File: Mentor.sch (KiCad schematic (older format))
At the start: 35 parts

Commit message: Mentor Schematic, V1.0
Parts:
- removed J?: CONN_01X04, symbol CONN_01X04
- added J2: CONN_01X05, symbol CONN_01X05
- added J7: CONN_01X18, symbol CONN_01X18
- added R9: 100R, symbol R
- added RV1: 10k, symbol POT
- gave numbers to parts that had none: 34
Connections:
- wire segments 114 -> 129
- no-connect marks 1 -> 6
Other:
- note added: "4x40 Display"
- note added: "DB0"
- note added: "DB1"
- note added: "DB2"
- note added: "DB3"
- note added: "DB4"
- note added: "DB5"
- note added: "DB6"
- note added: "DB7\n"
- note added: "E1"
- note added: "E2"
- note added: "From Alexandrie\nControl board"
- note added: "LedA"
- note added: "LedK"
- note added: "Mentor"
- note added: "Mentor\nA power/U/I/VSWR/Temp. indicator\nfor the Hermes SDR familly"
- note added: "PTT\ndisable"
- note added: "RS\n"
- note added: "RW\n"
- note added: "VO"
- note added: "VSS"
- note added: "Vdd"
- note added: "Vee"
- note removed: "Alexandrite"
- note removed: "Alexandrite, the ever changing color gem \nA power/U/I/VSWR/Temp. indicator\nfor the Hermes SDR familly"
- note removed: "From TX/RX_Relay\nControl board"
- note removed: "reporter\n le pinout \nsur ctrl board \nAlexandrie\n"

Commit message: final schematic drawing
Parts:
- removed J2: CONN_01X05, symbol CONN_01X05
- removed J3: CONN_01X03, symbol CONN_01X03
- added J2: CONN_01X06, symbol CONN_01X06
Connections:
- wire segments 129 -> 134
- no-connect marks 6 -> 17
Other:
- note added: "<--C°"
- note added: "<--I"
- note added: "<--U"
- note added: "From Amp"
- note added: "Mentor\nA power/U/I/VSWR/Temp. indicator\nand security system\nfor the Hermes SDR familly"
- note added: "ptt disable/\n <-- Active Bias\n"
- note removed: "Mentor\nA power/U/I/VSWR/Temp. indicator\nfor the Hermes SDR familly"
- note removed: "ptt disable\n"
- moved on the sheet: L1, R1

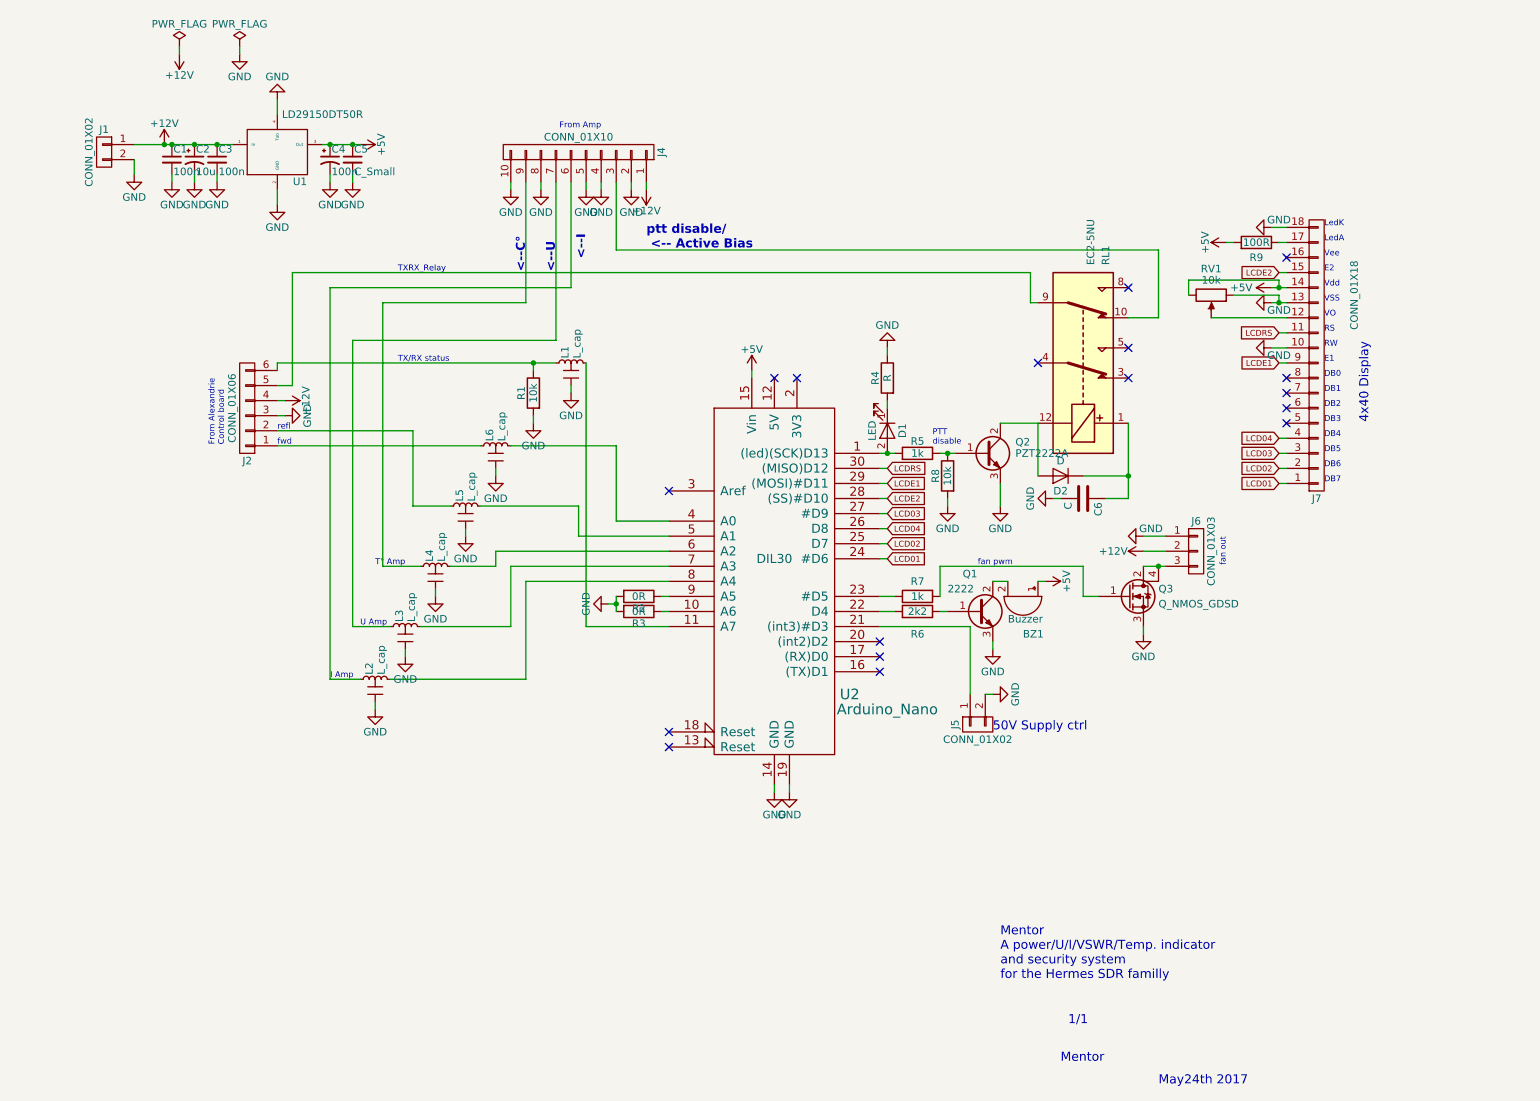
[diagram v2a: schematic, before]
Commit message: Mentor pcb routed, minor errors fixed
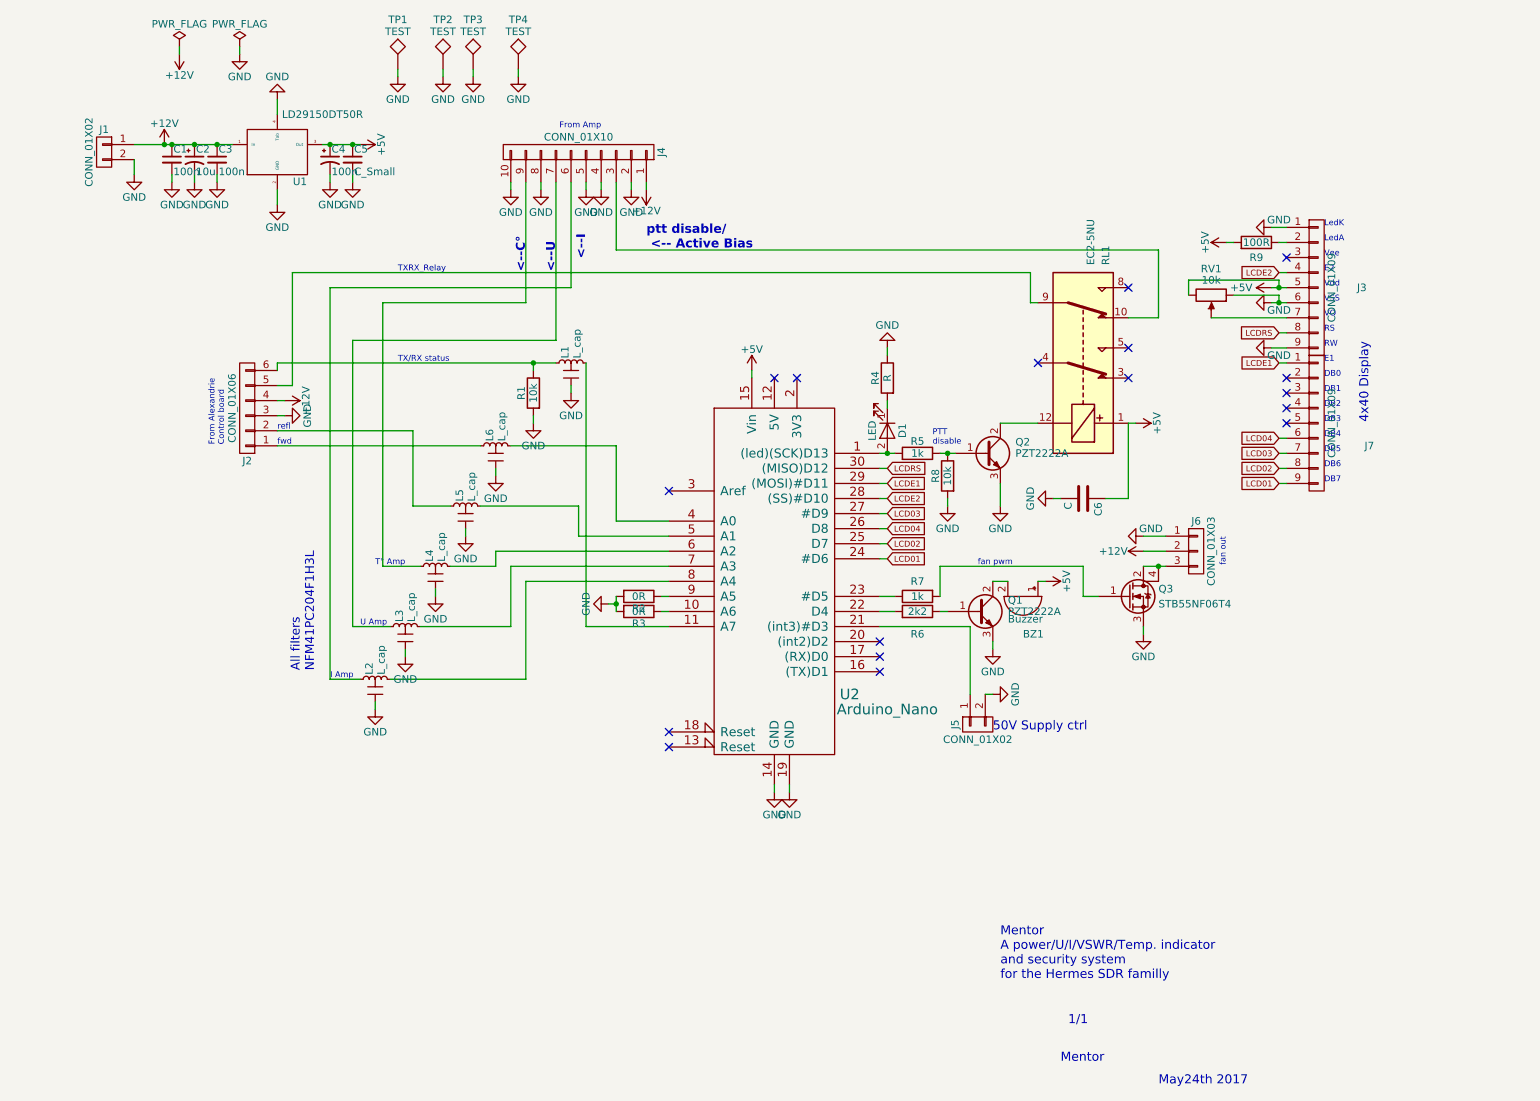
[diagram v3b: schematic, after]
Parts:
- removed D2: D, symbol D
- removed J7: CONN_01X18, symbol CONN_01X18
- added J3, J7: CONN_01X09, conn_kk100:kk100_22-23-2091, symbol CONN_01X09
- added TP1, TP2, TP3, TP4: TEST, Mounting_Holes:MountingHole_3.5mm_Pad, symbol TEST
- BZ1: footprint (none) -> Buzzers_Beepers:MagneticBuzzer_Kingstate_KCG0601
- C1, C3, C4, C5, C6: footprint (none) -> Capacitors_SMD:C_0805_HandSoldering
- C2: footprint (none) -> Capacitors_Tantalum_SMD:CP_Tantalum_Case-C_EIA-6032-28_Hand
- D1: footprint (none) -> Diodes_SMD:D_0805
- J1, J5: footprint (none) -> conn_kk100:kk100_22-23-2021
- J2: footprint (none) -> conn_kk100:kk100_22-23-2061
- J4: footprint (none) -> conn_kk100:kk100_22-23-2101
- J6: footprint (none) -> conn_kk100:kk100_22-23-2031
- L1, L2, L3, L4, L5, L6: footprint (none) -> Ferrite_LC_NFM41P:Ferrite_LC_NFM41P
- Q1: value 2222 -> PZT2222A
- Q3: value Q_NMOS_GDSD -> STB55NF06T4; footprint (none) -> TO_SOT_Packages_SMD:TO-263-3_TabPin4
- R1, R2, R3, R4, R5, R6, R7, R8, R9: footprint (none) -> Resistors_SMD:R_0805_HandSoldering
- RL1: footprint (none) -> 2_Form_C_Relay:smd_2_formC
- RV1: footprint (none) -> Trimmer_3314G1_Handsoldering:Trimmer_3314G1_Handsoldering
- U1: footprint (none) -> TO_SOT_Packages_SMD:SOT-223
- U2: footprint DIL30 -> arduino_nano:arduino_nano
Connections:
- net +5V: now also C6.1, RL1.1, J3.5 (P5)
- net GND: now also J3.1 (P1), J3.6 (P6), J3.9 (P9), TP1.1, TP2.1, TP3.1, TP4.1
- net LCD01: now also J7.9 (P9)
- net LCD02: now also J7.8 (P8)
- net LCD03: now also J7.7 (P7)
- net LCD04: now also J7.6 (P6)
- net LCDE1: now also J7.1 (P1)
- net LCDE2: now also J3.4 (P4)
- net LCDRS: now also J3.8 (P8)
- net at RV1.2: now also J3.7 (P7)
- net at R9.1: now also J3.2 (P2)
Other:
- note added: "All filters \nNFM41PC204F1H3L\n"

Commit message: RTM, silmask to do
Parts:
- C5: value C_Small -> 100n
- U1: footprint TO_SOT_Packages_SMD:SOT-223 -> TO_SOT_Packages_SMD:TO-263-3_TabPin4
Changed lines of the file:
@@
 F 0 "U1" H 2400 1254 50  0000 C CNN
 F 1 "LD29150DT50R" H 2550 1700 50  0000 C CNN
-F 2 "TO_SOT_Packages_SMD:SOT-223" H 2250 1450 50  0001 C CNN
+F 2 "TO_SOT_Packages_SMD:TO-263-3_TabPin4" H 2250 1450 50  0001 C CNN
 F 3 "" H 2250 1450 50  0001 C CNN
 	1    2250 1450
@@
 P 2750 1500
 F 0 "C5" H 2760 1570 50  0000 L CNN
-F 1 "C_Small" H 2760 1420 50  0000 L CNN
+F 1 "100n" H 2760 1420 50  0000 L CNN
 F 2 "Capacitors_SMD:C_0805_HandSoldering" H 2750 1500 50  0001 C CNN
 F 3 "" H 2750 1500 50  0001 C CNN

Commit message: carte de control V1.0
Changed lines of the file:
@@
 P 9150 2350
 F 0 "J3" H 9450 2350 50  0000 C CNN
-F 1 "CONN_01X09" V 9250 2350 50  0000 C CNN
+F 1 "CONN_01X09" V 9800 2300 50  0000 C CNN
 F 2 "conn_kk100:kk100_22-23-2091" H 9150 2350 50  0001 C CNN
 F 3 "" H 9150 2350 50  0001 C CNN

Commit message: add a THT relay, cleaning silk, shielding mask zone added
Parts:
- RL1: footprint 2_Form_C_Relay:smd_2_formC -> 2_Form_C_Relay:THT_2_formC
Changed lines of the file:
@@
 F 0 "RL1" H 8450 3200 50  0000 L CNN
 F 1 "EC2-5NU" H 8450 3100 50  0000 L CNN
-F 2 "2_Form_C_Relay:smd_2_formC" H 7600 3050 50  0001 C CNN
+F 2 "2_Form_C_Relay:THT_2_formC" H 7600 3050 50  0001 C CNN
 F 3 "" H 7600 3050 50  0001 C CNN
 	1    7600 3050

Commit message: RTM 1
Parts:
- RL1: value EC2-5NU -> EE2-12NU
- U1: value LD29150DT50R -> LD29150DT50R/ 78M05
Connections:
- net +12V: now also C6.1, RL1.1
- net +5V: no longer C6.1, RL1.1
- net at J4.3 (P3), RL1.10: now also RL1.3
- net at RL1.4: now also J2.5 (P5), RL1.9
- no-connect marks 17 -> 15
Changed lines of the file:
@@
 U 1 1 5924667F
 P 5550 4100
-F 0 "U2" H 6050 3150 70  0000 C CNN
-F 1 "Arduino_Nano" H 6300 3050 70  0000 C CNN
+F 0 "U2" H 5550 4050 70  0000 C CNN
+F 1 "Arduino_Nano" H 5550 3100 70  0000 C CNN
 F 2 "arduino_nano:arduino_nano" H 5550 4050 60  0001 C CNN
 F 3 "" H 5550 4100 60  0000 C CNN
@@
 U 1 1 5925303B
 P 7600 3050
-F 0 "RL1" H 8450 3200 50  0000 L CNN
-F 1 "EC2-5NU" H 8450 3100 50  0000 L CNN
+F 0 "RL1" V 8450 3000 50  0000 L CNN
+F 1 "EE2-12NU" V 7600 2850 50  0000 L CNN
 F 2 "2_Form_C_Relay:THT_2_formC" H 7600 3050 50  0001 C CNN
 F 3 "" H 7600 3050 50  0001 C CNN
@@
 	7900 2550 8100 2550
 Wire Wire Line
-	8100 2550 8100 2100
+	8100 2100 8100 2950
 Wire Wire Line
 	8100 2100 4500 2100
@@
 $EndComp
 Wire Wire Line
-	7250 2250 7250 2450
+	7250 2250 7250 2850
 Wire Wire Line
 	2350 2250 7250 2250
@@
 P 2250 1450
 F 0 "U1" H 2400 1254 50  0000 C CNN
-F 1 "LD29150DT50R" H 2550 1700 50  0000 C CNN
+F 1 "LD29150DT50R/ 78M05" H 2200 1750 50  0000 C CNN
 F 2 "TO_SOT_Packages_SMD:TO-263-3_TabPin4" H 2250 1450 50  0001 C CNN
 F 3 "" H 2250 1450 50  0001 C CNN
@@
 NoConn ~ 7900 2350
 NoConn ~ 7900 2750
-NoConn ~ 7900 2950
-NoConn ~ 7300 2850
 NoConn ~ 4850 3700
 NoConn ~ 5550 2950
@@
 Text Notes 2500 4900 1    59   ~ 0
 All filters \nNFM41PC204F1H3L\n
-$Comp
-L +5V #PWR049
-U 1 1 5929CBD0
-P 7950 3250
-F 0 "#PWR049" H 7950 3100 50  0001 C CNN
-F 1 "+5V" H 7950 3390 50  0000 C CNN
-F 2 "" H 7950 3250 50  0001 C CNN
-F 3 "" H 7950 3250 50  0001 C CNN
-	1    7950 3250
-	0    1    1    0
-$EndComp
 Wire Wire Line
 	7950 3250 7900 3250
@@
 $EndComp
 $Comp
-L GND #PWR050
+L GND #PWR049
 U 1 1 5929E680
 P 3850 950
-F 0 "#PWR050" H 3850 700 50  0001 C CNN
+F 0 "#PWR049" H 3850 700 50  0001 C CNN
 F 1 "GND" H 3850 800 50  0000 C CNN
 F 2 "" H 3850 950 50  0001 C CNN
@@
 	3850 900  3850 950
 $Comp
-L GND #PWR051
+L GND #PWR050
 U 1 1 5929E7F8
 P 3050 950
-F 0 "#PWR051" H 3050 700 50  0001 C CNN
+F 0 "#PWR050" H 3050 700 50  0001 C CNN
 F 1 "GND" H 3050 800 50  0000 C CNN
 F 2 "" H 3050 950 50  0001 C CNN
@@
 	3050 900  3050 950
 $Comp
-L GND #PWR052
+L GND #PWR051
 U 1 1 5929E82A
 P 3350 950
-F 0 "#PWR052" H 3350 700 50  0001 C CNN
+F 0 "#PWR051" H 3350 700 50  0001 C CNN
 F 1 "GND" H 3350 800 50  0000 C CNN
 F 2 "" H 3350 950 50  0001 C CNN
@@
 	3350 900  3350 950
 $Comp
-L GND #PWR053
+L GND #PWR052
 U 1 1 5929E885
 P 3550 950
-F 0 "#PWR053" H 3550 700 50  0001 C CNN
+F 0 "#PWR052" H 3550 700 50  0001 C CNN
 F 1 "GND" H 3550 800 50  0000 C CNN
 F 2 "" H 3550 950 50  0001 C CNN
@@
 Wire Wire Line
 	3550 900  3550 950
+$Comp
+L +12V #PWR053
+U 1 1 597CBD60
+P 7950 3250
+F 0 "#PWR053" H 7950 3100 50  0001 C CNN
+F 1 "+12V" H 7950 3390 50  0000 C CNN
+F 2 "" H 7950 3250 50  0001 C CNN
+F 3 "" H 7950 3250 50  0001 C CNN
+	1    7950 3250
+	0    1    1    0
+$EndComp
+Wire Wire Line
+	7250 2850 7300 2850
+Connection ~ 7250 2450
+Wire Wire Line
+	8100 2950 7900 2950
+Connection ~ 8100 2550
 $EndSCHEMATC

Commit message: new ferrite footprint, minor routing changes
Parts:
- removed Q3: STB55NF06T4, TO_SOT_Packages_SMD:TO-263-3_TabPin4, symbol Q_NMOS_GDSD
- removed U1: LD29150DT50R/ 78M05, TO_SOT_Packages_SMD:TO-263-3_TabPin4, symbol 7805D-Pack
- added Q3: IRFR3303, TO_SOT_Packages_SMD:TO-252-3_TabPin2, symbol IRF3205
- added U1: KA78M05_TO252, TO_SOT_Packages_SMD:TO-252-3_TabPin2, symbol KA78M05_TO252
- RL1: value EE2-12NU -> EC2-12NU
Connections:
- net +12V: now also U1.1 (VI)
- net +5V: now also U1.3 (VO)
- net GND: now also Q3.3 (S), U1.2 (GND)
- net at R6.2: now also Q3.1 (G)
- net at J6.3 (P3): now also Q3.2 (D)
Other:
- note added: "Mentor\nA power/U/I/VSWR/Temp. indicator\nand security system\nBy ON7EQ\nfor the Hermes SDR familly"
- note removed: "Mentor\nA power/U/I/VSWR/Temp. indicator\nand security system\nfor the Hermes SDR familly"
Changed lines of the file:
@@
 P 7600 3050
 F 0 "RL1" V 8450 3000 50  0000 L CNN
-F 1 "EE2-12NU" V 7600 2850 50  0000 L CNN
+F 1 "EC2-12NU" V 7600 2850 50  0000 L CNN
 F 2 "2_Form_C_Relay:THT_2_formC" H 7600 3050 50  0001 C CNN
 F 3 "" H 7600 3050 50  0001 C CNN
@@
 Text Notes 1900 3400 1    39   ~ 0
 From Alexandrie\nControl board
-$Comp
-L Q_NMOS_GDSD Q3
-U 1 1 59255616
-P 7900 4400
-F 0 "Q3" H 8100 4450 50  0000 L CNN
-F 1 "STB55NF06T4" H 8100 4350 50  0000 L CNN
-F 2 "TO_SOT_Packages_SMD:TO-263-3_TabPin4" H 8100 4500 50  0001 C CNN
-F 3 "" H 7900 4400 50  0001 C CNN
-	1    7900 4400
-	1    0    0    -1
-$EndComp
 $Comp
 L R R6
@@
 	1600 750  1600 800
 $Comp
-L 7805D-Pack U1
-U 1 1 59265A55
-P 2250 1450
-F 0 "U1" H 2400 1254 50  0000 C CNN
-F 1 "LD29150DT50R/ 78M05" H 2200 1750 50  0000 C CNN
-F 2 "TO_SOT_Packages_SMD:TO-263-3_TabPin4" H 2250 1450 50  0001 C CNN
-F 3 "" H 2250 1450 50  0001 C CNN
-	1    2250 1450
-	1    0    0    -1
-$EndComp
-$Comp
 L C_Small C1
 U 1 1 59265C31
@@
 Wire Wire Line
 	3900 4300 4850 4300
-Text Notes 7050 6950 0    60   ~ 0
-Mentor\nA power/U/I/VSWR/Temp. indicator\nand security system\nfor the Hermes SDR familly
+Text Notes 7100 7050 0    60   ~ 0
+Mentor\nA power/U/I/VSWR/Temp. indicator\nand security system\nBy ON7EQ\nfor the Hermes SDR familly
 Text Notes 7450 7500 0    60   ~ 0
 Mentor
@@
 Wire Wire Line
 	2250 1700 2250 1800
-$Comp
-L GND #PWR042
-U 1 1 5925758C
-P 2250 1100
-F 0 "#PWR042" H 2250 850 50  0001 C CNN
-F 1 "GND" H 2250 950 50  0000 C CNN
-F 2 "" H 2250 1100 50  0001 C CNN
-F 3 "" H 2250 1100 50  0001 C CNN
-	1    2250 1100
-	1    0    0    1
-$EndComp
-Wire Wire Line
-	2250 1200 2250 1100
 Wire Wire Line
 	3150 3300 2250 3300
@@
 	2300 3200 2250 3200
 $Comp
-L +12V #PWR043
+L +12V #PWR042
 U 1 1 5925C70F
 P 2300 3100
-F 0 "#PWR043" H 2300 2950 50  0001 C CNN
+F 0 "#PWR042" H 2300 2950 50  0001 C CNN
 F 1 "+12V" H 2300 3240 50  0000 C CNN
 F 2 "" H 2300 3100 50  0001 C CNN
@@
 	2300 3100 2250 3100
 $Comp
-L +5V #PWR044
+L +5V #PWR043
 U 1 1 5925A35B
 P 8850 2350
-F 0 "#PWR044" H 8850 2200 50  0001 C CNN
+F 0 "#PWR043" H 8850 2200 50  0001 C CNN
 F 1 "+5V" V 8850 2550 50  0000 C CNN
 F 2 "" H 8850 2350 50  0001 C CNN
@@
 $EndComp
 $Comp
-L GND #PWR045
+L GND #PWR044
 U 1 1 5925A8DD
 P 8850 2450
-F 0 "#PWR045" H 8850 2200 50  0001 C CNN
+F 0 "#PWR044" H 8850 2200 50  0001 C CNN
 F 1 "GND" V 8800 2500 50  0000 C CNN
 F 2 "" H 8850 2450 50  0001 C CNN
@@
 $EndComp
 $Comp
-L GND #PWR046
+L GND #PWR045
 U 1 1 5925FC2C
 P 8850 1950
-F 0 "#PWR046" H 8850 1700 50  0001 C CNN
+F 0 "#PWR045" H 8850 1700 50  0001 C CNN
 F 1 "GND" V 8900 2000 50  0000 C CNN
 F 2 "" H 8850 1950 50  0001 C CNN
@@
 	8950 2050 8900 2050
 $Comp
-L +5V #PWR047
+L +5V #PWR046
 U 1 1 5925FD3B
 P 8550 2050
-F 0 "#PWR047" H 8550 1900 50  0001 C CNN
+F 0 "#PWR046" H 8550 1900 50  0001 C CNN
 F 1 "+5V" H 8550 2190 50  0000 C CNN
 F 2 "" H 8550 2050 50  0001 C CNN
@@
 	8950 3650 8900 3650
 $Comp
-L GND #PWR048
+L GND #PWR047
 U 1 1 592BC3C5
 P 8850 2750
-F 0 "#PWR048" H 8850 2500 50  0001 C CNN
+F 0 "#PWR047" H 8850 2500 50  0001 C CNN
 F 1 "GND" V 8800 2800 50  0000 C CNN
 F 2 "" H 8850 2750 50  0001 C CNN
@@
 $EndComp
 $Comp
-L GND #PWR049
+L GND #PWR048
 U 1 1 5929E680
 P 3850 950
-F 0 "#PWR049" H 3850 700 50  0001 C CNN
+F 0 "#PWR048" H 3850 700 50  0001 C CNN
 F 1 "GND" H 3850 800 50  0000 C CNN
 F 2 "" H 3850 950 50  0001 C CNN
@@
 	3850 900  3850 950
 $Comp
-L GND #PWR050
+L GND #PWR049
 U 1 1 5929E7F8
 P 3050 950
-F 0 "#PWR050" H 3050 700 50  0001 C CNN
+F 0 "#PWR049" H 3050 700 50  0001 C CNN
 F 1 "GND" H 3050 800 50  0000 C CNN
 F 2 "" H 3050 950 50  0001 C CNN
@@
 	3050 900  3050 950
 $Comp
-L GND #PWR051
+L GND #PWR050
 U 1 1 5929E82A
 P 3350 950
-F 0 "#PWR051" H 3350 700 50  0001 C CNN
+F 0 "#PWR050" H 3350 700 50  0001 C CNN
 F 1 "GND" H 3350 800 50  0000 C CNN
 F 2 "" H 3350 950 50  0001 C CNN
@@
 	3350 900  3350 950
 $Comp
-L GND #PWR052
+L GND #PWR051
 U 1 1 5929E885
 P 3550 950
-F 0 "#PWR052" H 3550 700 50  0001 C CNN
+F 0 "#PWR051" H 3550 700 50  0001 C CNN
 F 1 "GND" H 3550 800 50  0000 C CNN
 F 2 "" H 3550 950 50  0001 C CNN
@@
 	3550 900  3550 950
 $Comp
-L +12V #PWR053
+L +12V #PWR052
 U 1 1 597CBD60
 P 7950 3250
-F 0 "#PWR053" H 7950 3100 50  0001 C CNN
+F 0 "#PWR052" H 7950 3100 50  0001 C CNN
 F 1 "+12V" H 7950 3390 50  0000 C CNN
 F 2 "" H 7950 3250 50  0001 C CNN
@@
 	8100 2950 7900 2950
 Connection ~ 8100 2550
+$Comp
+L KA78M05_TO252 U1
+U 1 1 5A158332
+P 2250 1400
+F 0 "U1" H 2100 1525 50  0000 C CNN
+F 1 "KA78M05_TO252" H 2250 1525 50  0000 L CNN
+F 2 "TO_SOT_Packages_SMD:TO-252-3_TabPin2" H 2250 1625 50  0001 C CIN
+F 3 "" H 2250 1350 50  0001 C CNN
+	1    2250 1400
+	1    0    0    -1
+$EndComp
+$Comp
+L IRF3205 Q3
+U 1 1 5A15886C
+P 7900 4400
+F 0 "Q3" H 8150 4475 50  0000 L CNN
+F 1 "IRFR3303" H 8150 4400 50  0000 L CNN
+F 2 "TO_SOT_Packages_SMD:TO-252-3_TabPin2" H 8150 4325 50  0001 L CIN
+F 3 "" H 7900 4400 50  0001 L CNN
+	1    7900 4400
+	1    0    0    -1
+$EndComp
 $EndSCHEMATC
